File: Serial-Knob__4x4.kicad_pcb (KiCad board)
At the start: 2 copper layers, 49 x 49 mm, 92 parts, among them IC1 ATTINY85-S, P1 CONN_4

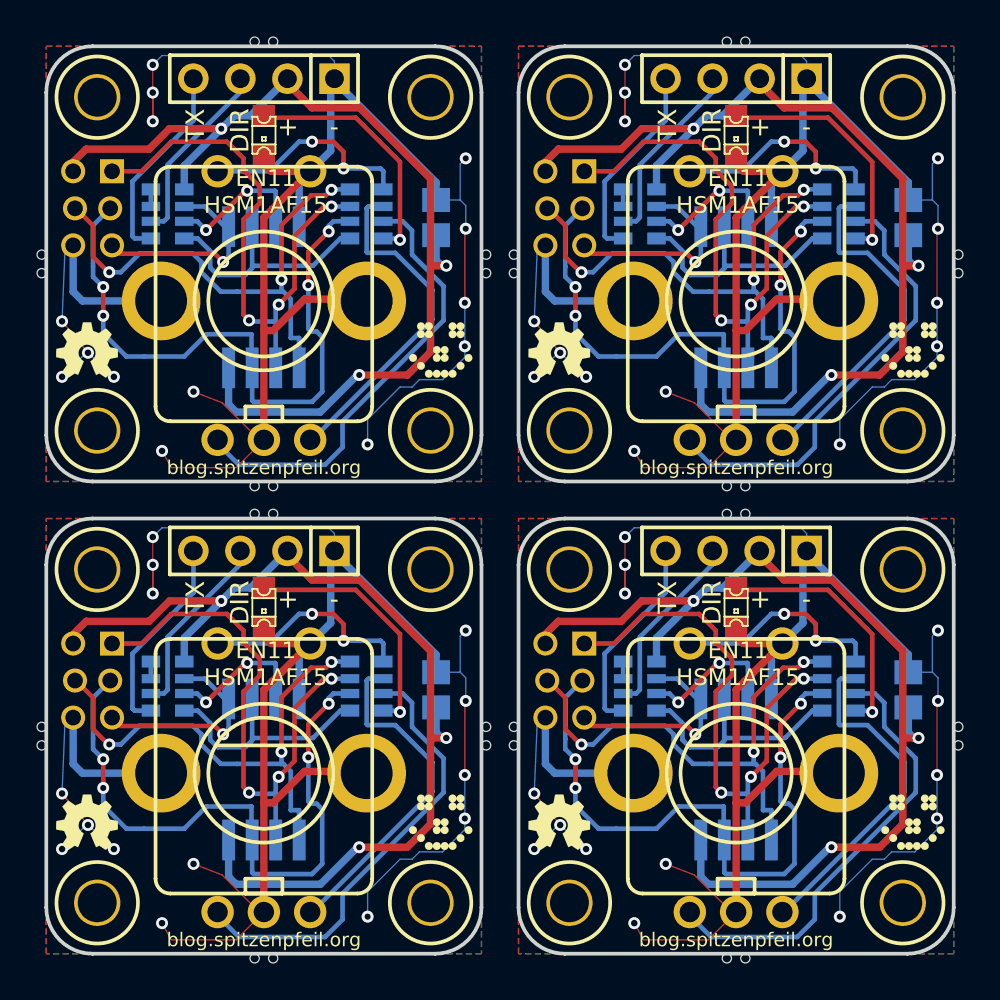
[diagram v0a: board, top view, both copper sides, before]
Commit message: Added more drills to the break-away tabs.
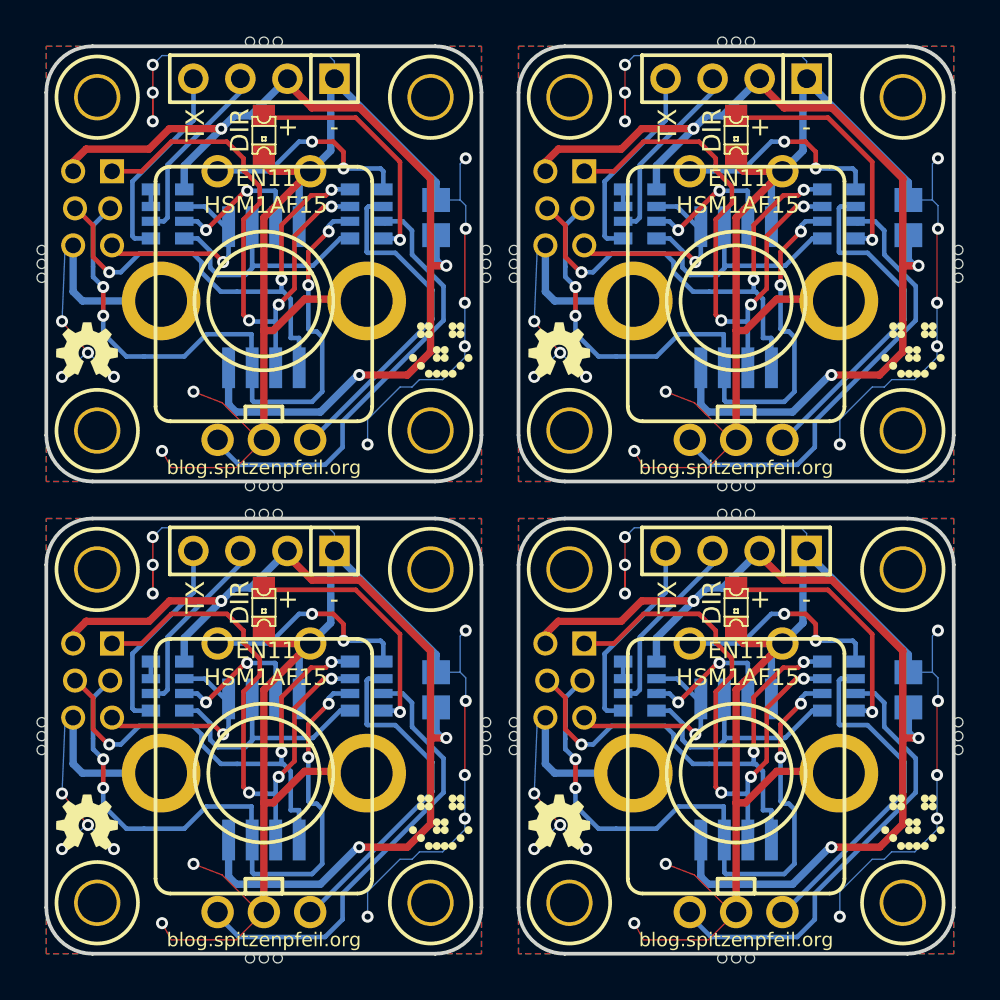
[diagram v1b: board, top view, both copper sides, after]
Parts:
- added 1PIN: P***, 1pin, F.Cu at (113.0, 82.5)
- added 1PIN: P***, 1pin, F.Cu at (87.5, 57.0)
- added 1PIN: P***, 1pin, F.Cu at (101.0, 45.0)
- added 1PIN: P***, 1pin, F.Cu at (125.0, 45.0)
- added 1PIN: P***, 1pin, F.Cu at (113.0, 33.0)
- added 1PIN: P***, 1pin, F.Cu at (99.5, 45.0)
- added 1PIN: P***, 1pin, F.Cu at (75.5, 45.0)
- added 1PIN: P***, 1pin, F.Cu at (87.5, 33.0)
- added 1PIN: P***, 1pin, F.Cu at (87.5, 82.5)
- added 1PIN: P***, 1pin, F.Cu at (125.0, 70.5)
- added 1PIN: P***, 1pin, F.Cu at (101.0, 70.5)
- added 1PIN: P***, 1pin, F.Cu at (99.5, 70.5)
- added 1PIN: P***, 1pin, F.Cu at (75.5, 70.5)
- added 1PIN: P***, 1pin, F.Cu at (113.0, 58.5)
- added 1PIN: P***, 1pin, F.Cu at (113.0, 57.0)
- added 1PIN: P***, 1pin, F.Cu at (87.5, 58.5)
- moved 1PIN 0.25 mm to (113.8, 57.0)
- moved 1PIN 0.25 mm to (101.0, 45.8)
- moved 1PIN 0.25 mm to (101.0, 44.2)
- moved 1PIN 0.25 mm to (125.0, 45.8)
- moved 1PIN 0.25 mm to (113.8, 33.0)
- moved 1PIN 0.25 mm to (125.0, 44.2)
- moved 1PIN 0.25 mm to (112.2, 57.0)
- moved 1PIN 0.25 mm to (112.2, 33.0)
- moved 1PIN 0.25 mm to (86.8, 33.0)
- moved 1PIN 0.25 mm to (86.8, 57.0)
- moved 1PIN 0.25 mm to (99.5, 44.2)
- moved 1PIN 0.25 mm to (88.2, 33.0)
- moved 1PIN 0.25 mm to (99.5, 45.8)
- moved 1PIN 0.25 mm to (75.5, 44.2)
- moved 1PIN 0.25 mm to (75.5, 45.8)
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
